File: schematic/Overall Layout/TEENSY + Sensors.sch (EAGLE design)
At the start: 17 parts, among them M7 SERVO, M8 SERVO, M9 SERVO, U1 MAX13054ASA, U6 55DEG, U7 55DEG

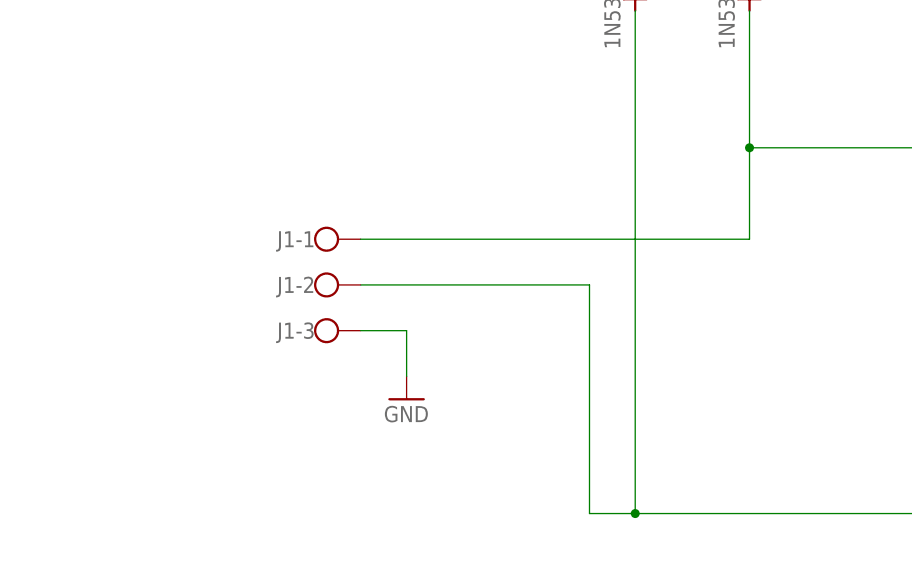
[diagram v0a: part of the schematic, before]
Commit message: Added military connectors to CAN Bus and added copper threading to PCB designs
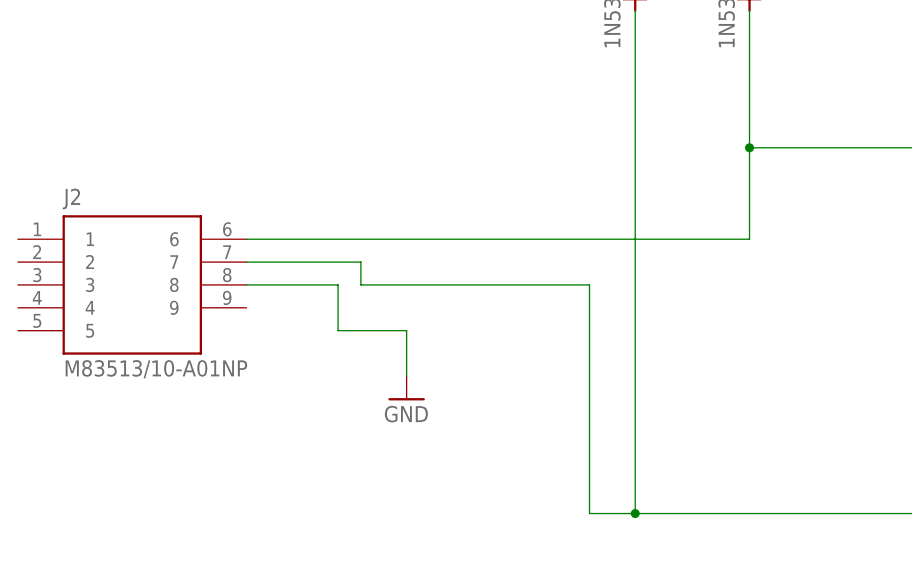
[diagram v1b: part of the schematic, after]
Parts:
- removed J1: (no value), con-wago-500:W237-103
- added J2: M83513/10-A01NP, M83513_10-A01NP:M83513/10-A01NP
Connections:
- net CAN_BUS: now also J2.6; no longer J1-1.KL
- net GND: now also J2.8; no longer J1-3.KL
- net N$5: now also J2.7; no longer J1-2.KL
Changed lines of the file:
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@@
 </variantdefs>
 <classes>
-<class number="0" name="default" width="0" drill="0">
+<class number="0" name="default" width="0.3048" drill="0.508">
+<clearance class="0" value="0.254"/>
 </class>
 </classes>
@@
 <part name="D3" library="diode" library_urn="urn:adsk.eagle:library:210" deviceset="1N5333" device="" package3d_urn="urn:adsk.eagle:package:43351/1"/>
 <part name="D4" library="diode" library_urn="urn:adsk.eagle:library:210" deviceset="1N5333" device="" package3d_urn="urn:adsk.eagle:package:43351/1"/>
-<part name="J1" library="con-wago-500" library_urn="urn:adsk.eagle:library:195" deviceset="W237-103" device="" package3d_urn="urn:adsk.eagle:package:10691/1"/>
 <part name="GND4" library="supply1" library_urn="urn:adsk.eagle:library:371" deviceset="GND" device=""/>
 <part name="GND5" library="supply1" library_urn="urn:adsk.eagle:library:371" deviceset="GND" device=""/>
@@
 <part name="SUPPLY23" library="SparkFun-PowerSymbols" deviceset="VCC" device=""/>
 <part name="SUPPLY24" library="SparkFun-PowerSymbols" deviceset="VCC" device=""/>
+<part name="J2" library="M83513_10-A01NP" deviceset="M83513/10-A01NP" device=""/>
 </parts>
 <sheets>
@@
 <attribute name="VALUE" x="46.609" y="135.382" size="1.778" layer="96" rot="R90"/>
 </instance>
-<instance part="J1" gate="-1" x="-5.08" y="99.06" smashed="yes">
-<attribute name="NAME" x="-5.08" y="99.949" size="1.778" layer="95" rot="R180"/>
-</instance>
-<instance part="J1" gate="-2" x="-5.08" y="93.98" smashed="yes">
-<attribute name="NAME" x="-5.08" y="94.869" size="1.778" layer="95" rot="R180"/>
-</instance>
-<instance part="J1" gate="-3" x="-5.08" y="88.9" smashed="yes">
-<attribute name="VALUE" x="-7.62" y="85.217" size="1.778" layer="96"/>
-<attribute name="NAME" x="-5.08" y="89.789" size="1.778" layer="95" rot="R180"/>
-</instance>
 <instance part="GND4" gate="1" x="38.1" y="147.32" smashed="yes" rot="R180">
 <attribute name="VALUE" x="40.64" y="149.86" size="1.778" layer="96" rot="R180"/>
@@
 <instance part="SUPPLY24" gate="G$1" x="208.28" y="-17.78" smashed="yes" rot="R270">
 <attribute name="VALUE" x="211.074" y="-17.78" size="1.778" layer="96" rot="R270" align="bottom-center"/>
+</instance>
+<instance part="J2" gate="G$1" x="-25.4" y="93.98" smashed="yes">
+<attribute name="NAME" x="-33.02" y="102.87" size="1.778" layer="95"/>
+<attribute name="VALUE" x="-33.02" y="83.82" size="1.778" layer="96"/>
 </instance>
 </instances>
@@
 </segment>
 <segment>
-<pinref part="J1" gate="-3" pin="KL"/>
-<wire x1="0" y1="88.9" x2="5.08" y2="88.9" width="0.1524" layer="91"/>
+<wire x1="-2.54" y1="88.9" x2="5.08" y2="88.9" width="0.1524" layer="91"/>
 <pinref part="GND5" gate="1" pin="GND"/>
 <wire x1="5.08" y1="88.9" x2="5.08" y2="83.82" width="0.1524" layer="91"/>
+<wire x1="-2.54" y1="88.9" x2="-2.54" y2="93.98" width="0.1524" layer="91"/>
+<pinref part="J2" gate="G$1" pin="8"/>
+<wire x1="-2.54" y1="93.98" x2="-12.7" y2="93.98" width="0.1524" layer="91"/>
 </segment>
 <segment>
@@
 <wire x1="30.48" y1="124.46" x2="30.48" y2="68.58" width="0.1524" layer="91"/>
 <wire x1="30.48" y1="68.58" x2="66.04" y2="68.58" width="0.1524" layer="91"/>
-<pinref part="J1" gate="-2" pin="KL"/>
 <wire x1="0" y1="93.98" x2="25.4" y2="93.98" width="0.1524" layer="91"/>
 <wire x1="25.4" y1="93.98" x2="25.4" y2="68.58" width="0.1524" layer="91"/>
@@
 <pinref part="U1" gate="A" pin="CANL"/>
 <wire x1="99.06" y1="104.14" x2="114.3" y2="104.14" width="0.1524" layer="91"/>
+<wire x1="0" y1="93.98" x2="0" y2="96.52" width="0.1524" layer="91"/>
+<pinref part="J2" gate="G$1" pin="7"/>
+<wire x1="0" y1="96.52" x2="-12.7" y2="96.52" width="0.1524" layer="91"/>
 </segment>
 </net>
@@
 <wire x1="43.18" y1="124.46" x2="43.18" y2="109.22" width="0.1524" layer="91"/>
 <wire x1="43.18" y1="109.22" x2="66.04" y2="109.22" width="0.1524" layer="91"/>
-<pinref part="J1" gate="-1" pin="KL"/>
-<wire x1="0" y1="99.06" x2="43.18" y2="99.06" width="0.1524" layer="91"/>
+<wire x1="-12.7" y1="99.06" x2="43.18" y2="99.06" width="0.1524" layer="91"/>
 <wire x1="43.18" y1="99.06" x2="43.18" y2="109.22" width="0.1524" layer="91"/>
 <junction x="43.18" y="109.22"/>
+<pinref part="J2" gate="G$1" pin="6"/>
 </segment>
 </net>
